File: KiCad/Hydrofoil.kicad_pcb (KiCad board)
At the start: 2 copper layers, 219.6 x 35 mm, 62 parts, among them J1 Conn_01x03_Pin, J2 Conn_01x03_Pin, Q1 BSS138, Q2 BSS138, Q3 BSS138, Q4 BSS138, Q5 BSS138, U1 ESP32-C3-MINI-1-N4, U2 LD1117S33CTR, U3 TPS22917DBV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

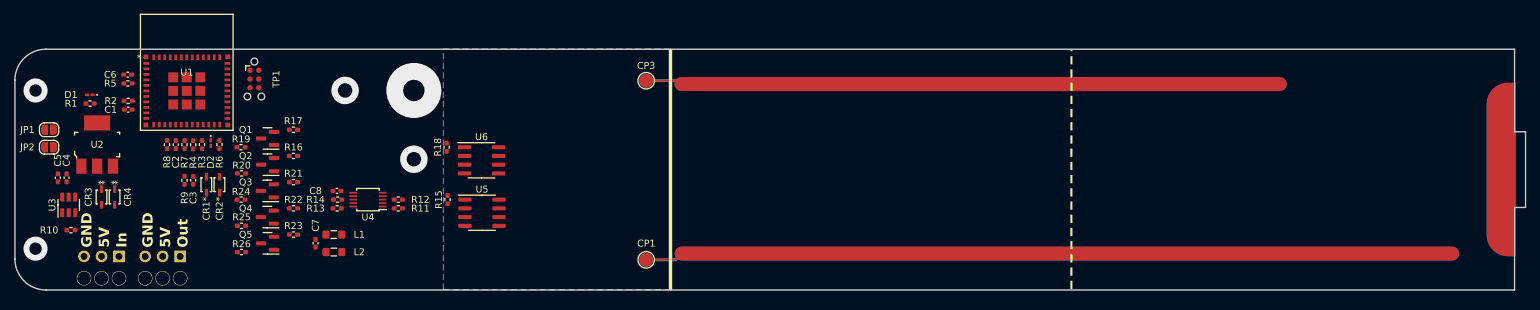
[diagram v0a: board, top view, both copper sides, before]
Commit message: Finish PCB layout, start PCB routing
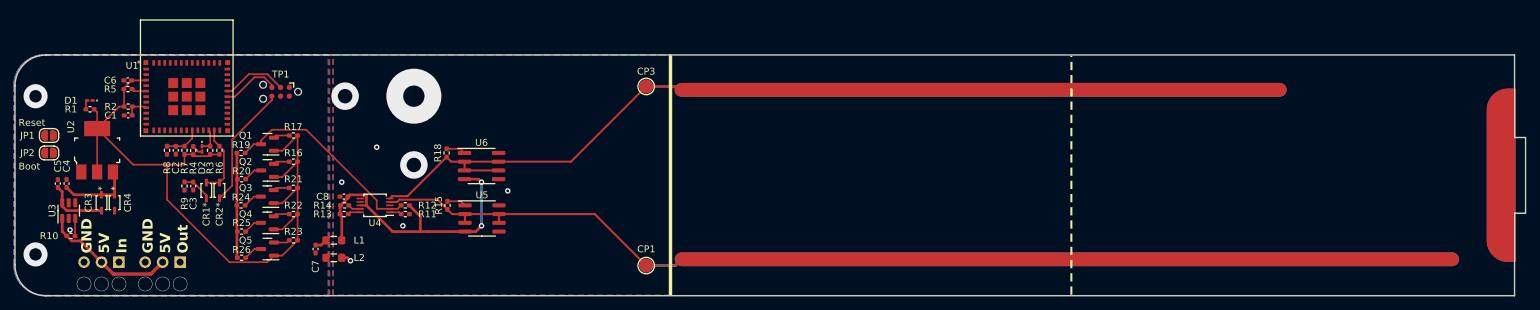
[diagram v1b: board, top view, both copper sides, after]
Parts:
- moved TP1 4.24 mm to (77.5, 77.0), turned to 180 degrees
- moved D2 1.52 mm to (66.0, 85.3)
- moved R3 1.46 mm to (67.2, 85.6)
- moved R12 1.32 mm to (95.6, 93.5)
- moved R14 1.32 mm to (86.8, 93.5)
- moved U4 1.32 mm to (91.2, 93.5)
- moved C8 1.32 mm to (86.7, 92.3)
- moved R11 1.32 mm to (95.6, 94.8)
- moved R13 1.32 mm to (86.7, 94.8)
- moved C4 0.83 mm to (46.4, 90.4)
- moved C5 0.83 mm to (45.1, 90.4)
- moved JP1 0.83 mm to (43.8, 83.4)
- moved Q1 0.83 mm to (75.6, 84.7)
- moved Q2 0.83 mm to (75.6, 88.5)
- moved R1 0.83 mm to (49.8, 79.6)
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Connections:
- net /ADS1115-ADC/SETcur1 renamed /ADS1115-ADC/Set-Curr-1
- net /ADS1115-ADC/SETcur2 renamed /ADS1115-ADC/Set-Curr-2
- R19 pad 1: +5VA -> +5V
- R20 pad 1: +5VA -> +5V
- R24 pad 1: +5VA -> +5V
- R25 pad 1: +5VA -> +5V
- R26 pad 1: +5VA -> +5V
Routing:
- net +3.3V: track 0.00 -> 104.5 mm
- net AIN1: track 92.3 -> 143.1 mm
- net +5VA: track 0.00 -> 44.3 mm, vias 0 -> 2
- net AIN0: track 117.5 -> 161.5 mm
- net Ready-HV: track 0.00 -> 30.1 mm
- net +5V: track 0.00 -> 26.0 mm
- net /+5V-Raw: track 0.00 -> 19.8 mm
- net ESP-Boot: track 0.00 -> 18.0 mm
- net /+5V-Logic: track 0.00 -> 10.8 mm
- net Input-Boot: track 0.00 -> 10.3 mm
- net ESP-Tx: track 0.00 -> 9.55 mm
- net ESP-Rx: track 0.00 -> 8.44 mm
- net Input-Reset: track 0.00 -> 5.31 mm
- net SCL-HV: track 0.00 -> 4.66 mm
- net SDA-HV: track 0.00 -> 4.63 mm
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- added copper zone on F.Cu, net GND
- added copper zone on B.Cu, net GNDA
- added copper zone on F.Cu, net GNDA
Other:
- board text added: "Boot"
- board text added: "Reset"

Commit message: Finish routing
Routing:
- net +5V: track 26.0 -> 66.7 mm, vias 0 -> 2
- net +5V-Prog: track 0.00 -> 39.2 mm, vias 0 -> 2
- net PWM-Out-LV: track 2.37 -> 31.8 mm, vias 0 -> 2
- net Ready-LV: track 2.37 -> 31.1 mm, vias 0 -> 2
- net PWM-In-LV: track 2.40 -> 29.9 mm, vias 0 -> 2
- net ESP-En: track 3.36 -> 27.8 mm, vias 0 -> 2
- net PWM-In-HV: track 2.73 -> 26.1 mm, vias 0 -> 1
- net SDA-HV: track 4.63 -> 27.5 mm, vias 0 -> 2
- net Net-(JP2-A): track 0.00 -> 21.4 mm, vias 0 -> 2
- net Net-(JP1-A): track 0.00 -> 17.6 mm, vias 0 -> 2
- net SCL-HV: track 4.66 -> 21.3 mm, vias 0 -> 2
- net SCL-LV: track 2.40 -> 17.7 mm, vias 0 -> 2
- net PWM-Out-HV: track 2.76 -> 16.9 mm, vias 0 -> 1
- net SDA-LV: track 2.37 -> 15.2 mm, vias 0 -> 2
- net AIN0: track 161.5 -> 164.5 mm
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- added copper zone on B.Cu, net (none)
- added copper zone on F.Cu, net (none)
